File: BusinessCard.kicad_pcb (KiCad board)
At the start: 4 copper layers, 88.9 x 50.8 mm, 80 parts, among them J1 USB_OTG, Q1 2N3904, Q2 2N3904, U1 TLE2426, U10 74HC74, U11 74HC74, U12 74HC74, U13 74HC74, U2 TLV271, U3 LM311, U4 74HC74, U5 INA826, U6 TLV272, U7 4066, U8 TLV272, U9 74HC14

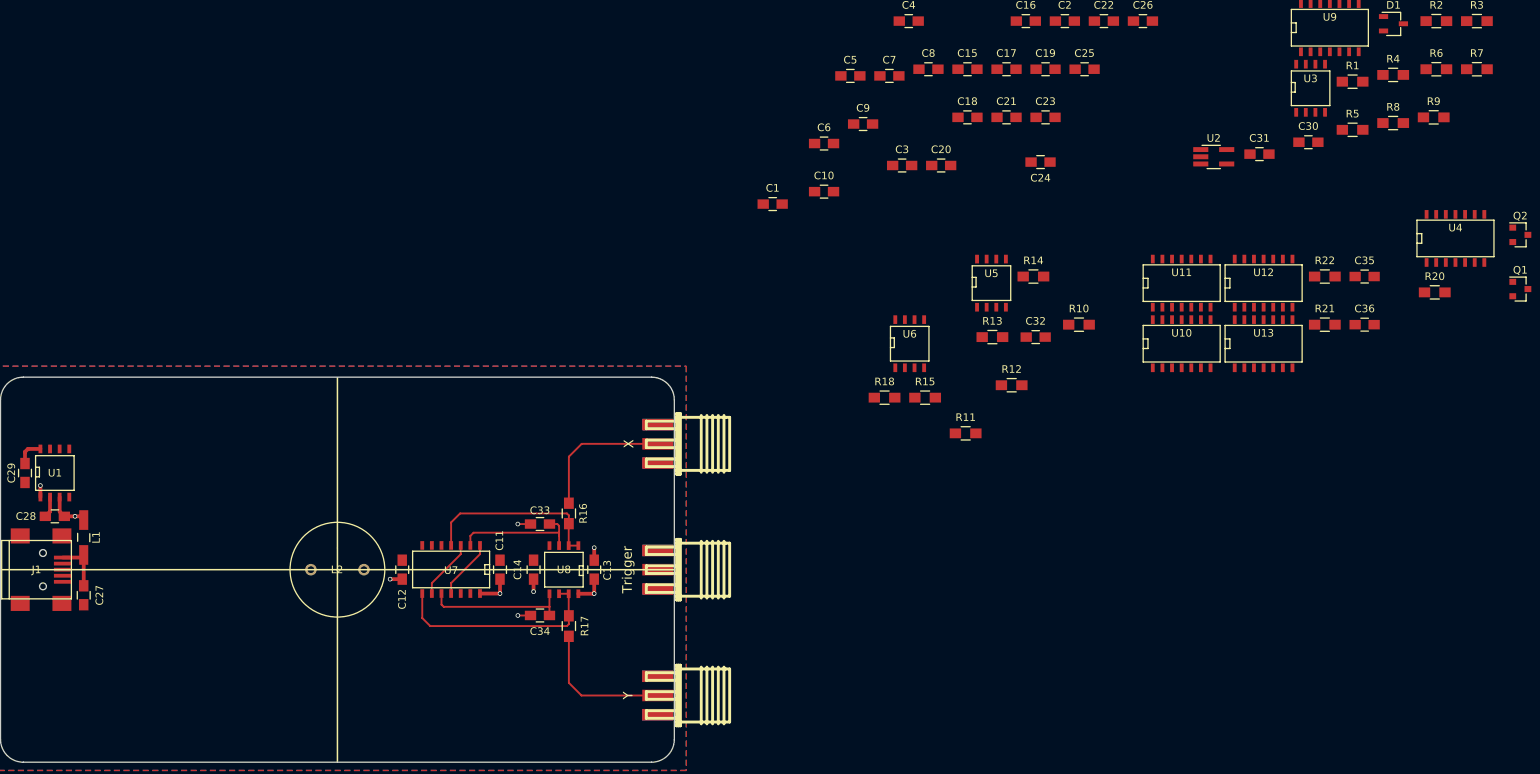
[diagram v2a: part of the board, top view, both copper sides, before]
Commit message: Fractal calculator placed.
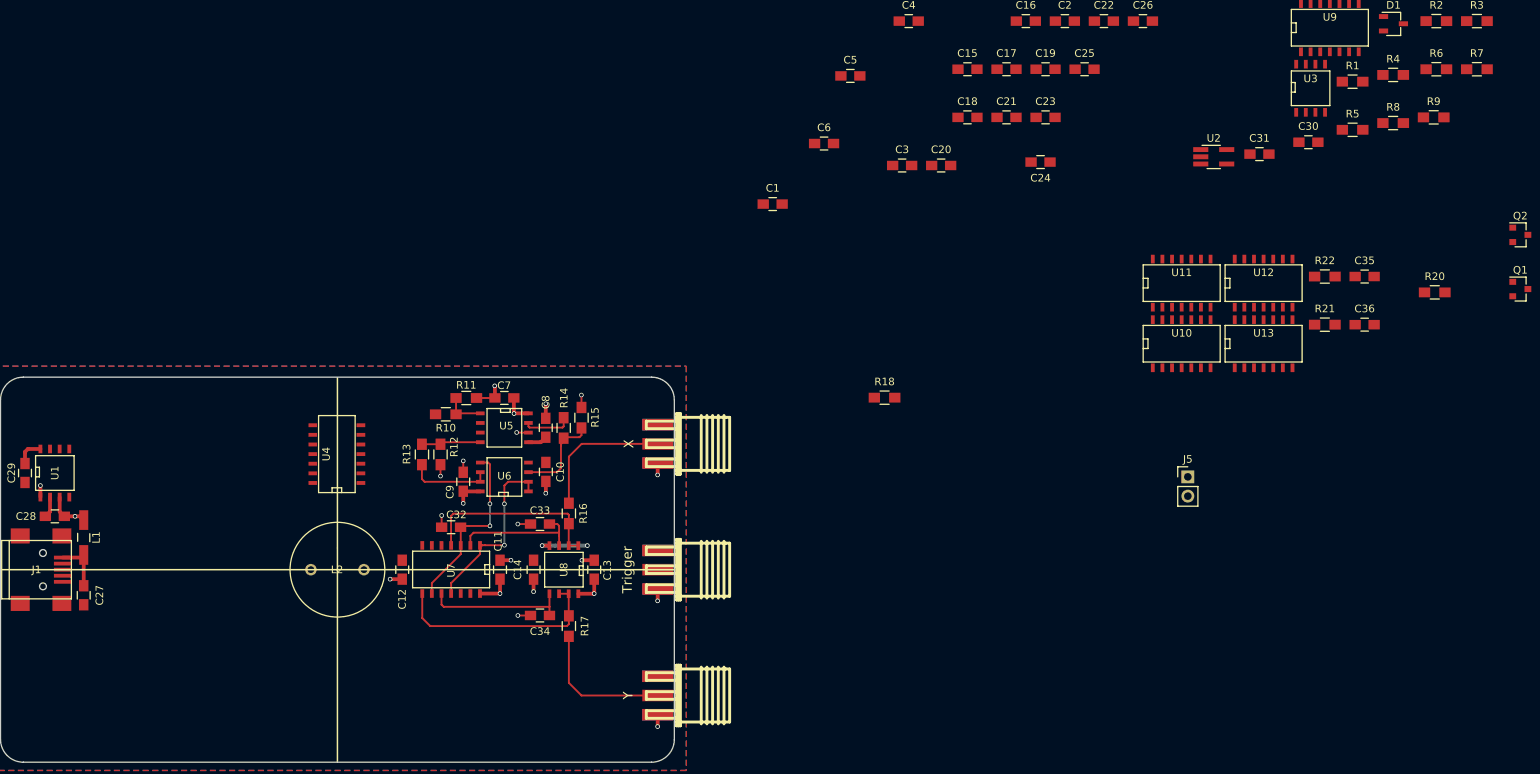
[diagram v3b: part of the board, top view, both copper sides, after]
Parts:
- added J5: RNG, Pin_Headers:Pin_Header_Straight_1x02_Pitch2.54mm, F.Cu at (261.7, 84.5)
- moved U4 150.4 mm to (149.3, 81.5), turned to 90 degrees
- moved R10 84.4 mm to (163.8, 76.2)
- moved C32 81.1 mm to (164.6, 91.1), turned to 180 degrees
- moved R13 76.8 mm to (160.7, 81.5), turned to 270 degrees
- moved R12 75.9 mm to (163.2, 81.5), turned to 270 degrees
- moved C9 70.8 mm to (166.2, 85.1), turned to 90 degrees
- moved C8 69.2 mm to (177.0, 78.0), turned to 270 degrees
- moved U5 67.0 mm to (171.6, 78.0), turned to 270 degrees
- moved C7 66.2 mm to (171.6, 74.0), turned to 180 degrees
- moved R11 66.0 mm to (166.6, 74.0)
- moved R14 65.1 mm to (179.4, 78.0), turned to 270 degrees
- moved U6 56.3 mm to (171.6, 84.5), turned to 90 degrees
- moved C10 52.1 mm to (177.1, 83.8), turned to 90 degrees
- moved R15 45.4 mm to (181.8, 76.7), turned to 90 degrees
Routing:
- net GNDREF: track 9.77 -> 31.6 mm, vias 6 -> 18
- net Net-(C32-Pad1): track 7.93 -> 23.8 mm, vias 0 -> 2
- net Net-(U6-Pad1): track 7.93 -> 23.7 mm, vias 0 -> 2
- net Net-(R14-Pad2): track 0.00 -> 12.1 mm
- net Net-(R13-Pad2): track 0.00 -> 11.1 mm
- net -VDC: track 2.79 -> 12.3 mm, vias 0 -> 2
- net +VDC: track 14.1 -> 22.2 mm, vias 3 -> 5
- net Net-(R12-Pad1): track 0.00 -> 7.81 mm
- net Net-(R14-Pad1): track 0.00 -> 6.38 mm
- net Net-(R10-Pad2): track 0.00 -> 5.40 mm
- net FRACTAL_X: track 24.4 -> 25.0 mm

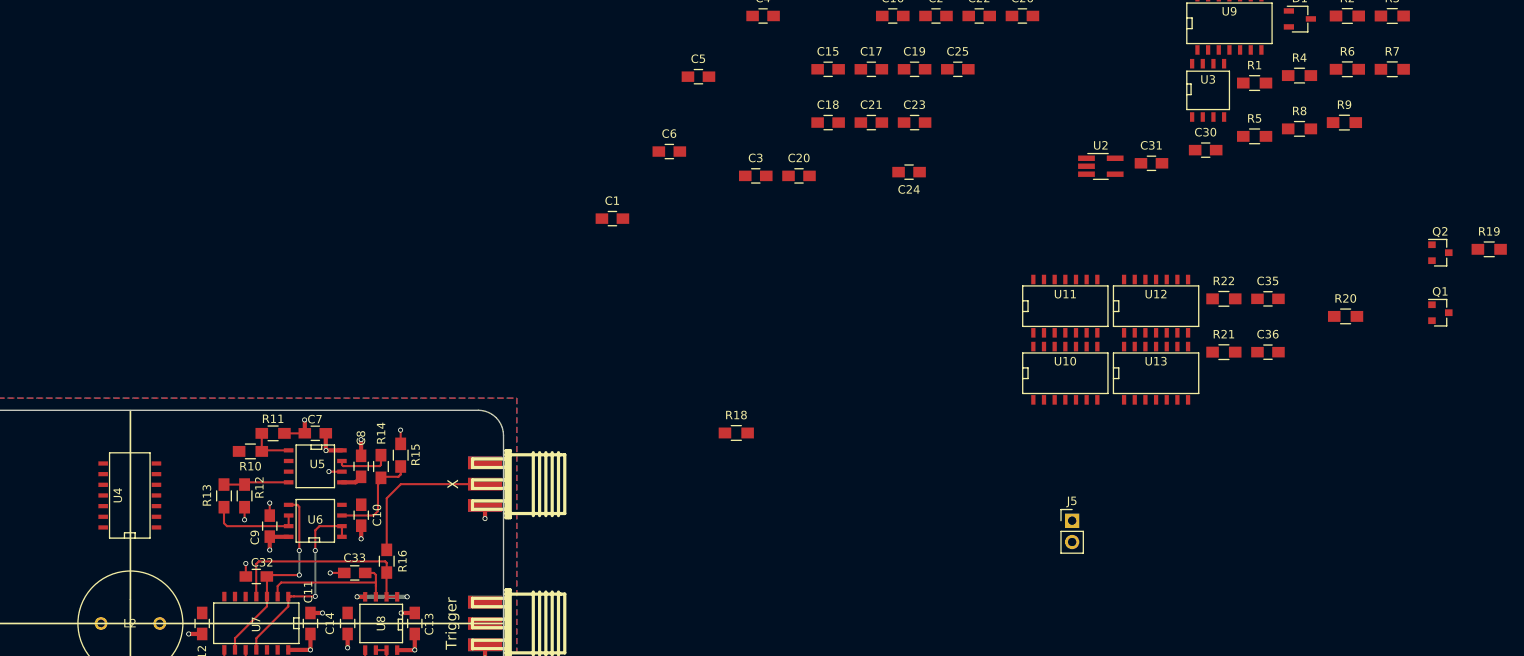
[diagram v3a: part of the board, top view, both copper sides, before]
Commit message: fractal coordinate selector placed.
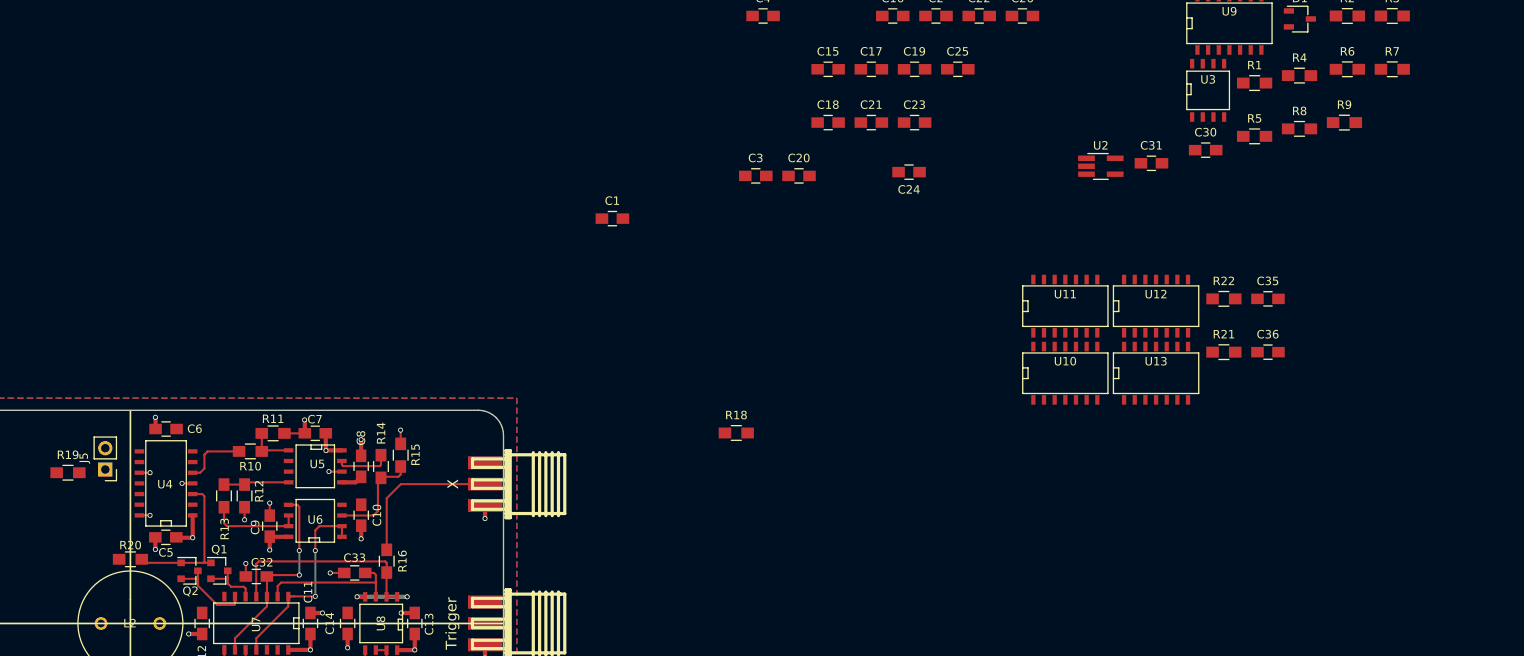
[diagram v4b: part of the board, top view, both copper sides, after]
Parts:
- moved R19 171.4 mm to (142.1, 78.7)
- moved Q2 153.8 mm to (156.6, 90.4)
- moved Q1 148.7 mm to (160.1, 90.4)
- moved R20 147.6 mm to (149.6, 89.1), turned to 180 degrees
- moved J5 115.4 mm to (146.6, 78.4), turned to 180 degrees
- moved C5 83.9 mm to (153.8, 86.4), turned to 180 degrees
- moved C6 68.5 mm to (153.8, 73.5)
- moved U4 4.55 mm to (153.7, 80.0)
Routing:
- net Net-(Q1-Pad1): track 0.00 -> 18.0 mm
- net CLOCK_CYCLE_2: track 0.00 -> 10.2 mm
- net +VDC: track 22.2 -> 30.6 mm, vias 5 -> 9
- net COORDINATE: track 0.00 -> 7.55 mm
- net CLOCK_CYCLE_0: track 0.00 -> 7.10 mm
- net GNDREF: track 31.6 -> 34.4 mm, vias 18 -> 20

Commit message: Started fractal clock placement
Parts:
- moved R7 188.1 mm to (119.0, 82.2), turned to 90 degrees
- moved C20 178.4 mm to (66.1, 115.8)
- moved C21 178.4 mm to (74.8, 109.4)
- moved C22 178.4 mm to (87.6, 96.7)
- moved C23 178.4 mm to (79.9, 109.4)
- moved C19 178.4 mm to (79.9, 103.1)
- moved C24 178.4 mm to (79.2, 115.3)
- moved R9 178.3 mm to (126.2, 96.8), turned to 90 degrees
- moved R3 173.1 mm to (135.9, 79.8), turned to 270 degrees
- moved C26 173.1 mm to (92.8, 82.5)
- moved R2 170.6 mm to (131.7, 75.1)
- moved U12 170.3 mm to (111.3, 115.8)
- moved C35 168.2 mm to (121.4, 96.8), turned to 90 degrees
- moved R8 167.5 mm to (125.5, 75.0)
- moved D1 166.9 mm to (131.3, 79.8), turned to 270 degrees
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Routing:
- net Net-(C31-Pad1): track 0.00 -> 25.7 mm
- net Net-(J5-Pad1): track 0.00 -> 24.7 mm, vias 0 -> 1
- net Net-(R6-Pad1): track 0.00 -> 21.7 mm
- net Net-(C30-Pad1): track 0.00 -> 20.5 mm, vias 0 -> 1
- net GNDREF: track 34.4 -> 52.7 mm, vias 20 -> 31
- net +VDC: track 30.6 -> 48.8 mm, vias 9 -> 14
- net Net-(C35-Pad1): track 0.00 -> 16.4 mm
- net RESET: track 0.00 -> 15.6 mm, vias 0 -> 2
- net CHUA_ATTRACTOR: track 0.00 -> 13.8 mm
- net CLOCK: track 0.00 -> 13.0 mm
- net Net-(R4-Pad1): track 0.00 -> 12.4 mm
- net Net-(R7-Pad2): track 0.00 -> 10.6 mm
- net FRACTAL_TRIGGER: track 0.00 -> 10.5 mm
- net CLOCK_CYCLE_0: track 7.10 -> 14.5 mm
- net Net-(R5-Pad2): track 0.00 -> 6.12 mm
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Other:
- board text added: "Craig Heffner (443) 896-7331 heffnercj@gmail.com"
- board text added: "code-free"
- board text added: "μC"

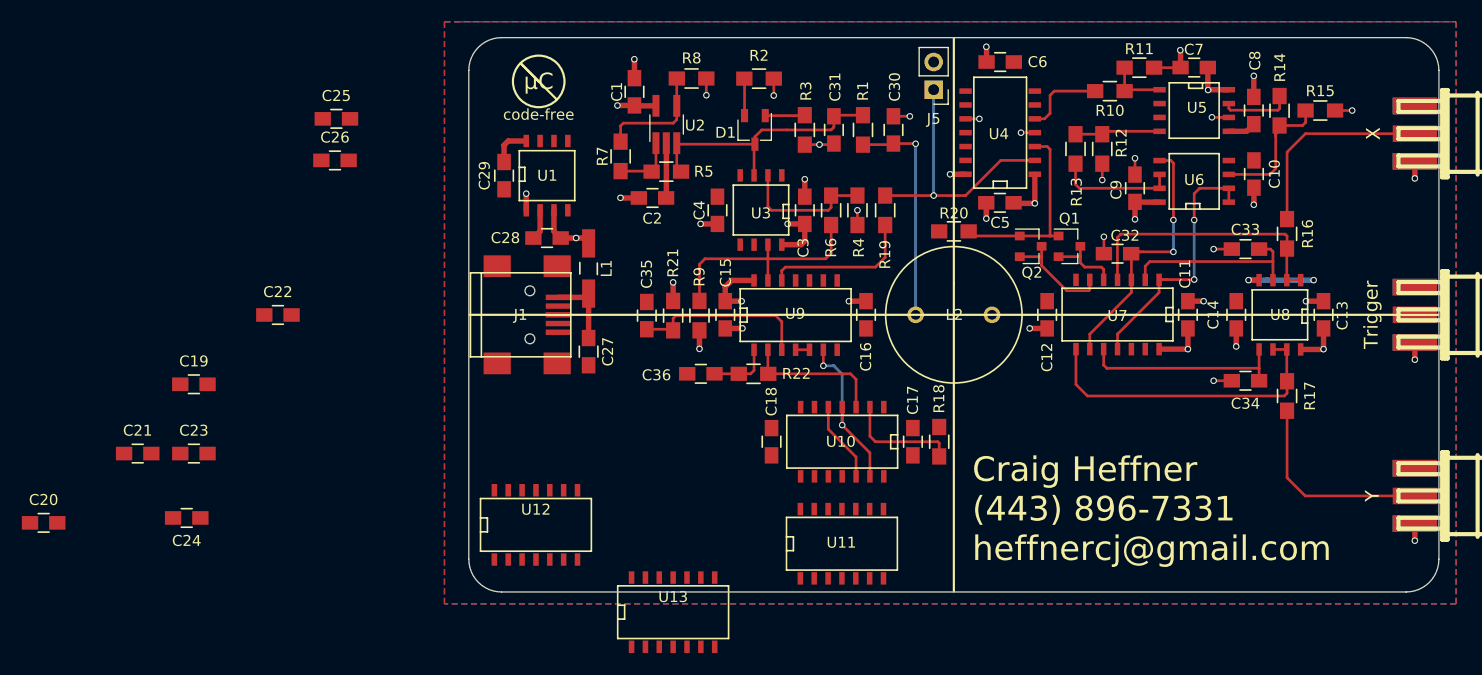
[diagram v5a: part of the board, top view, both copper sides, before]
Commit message: All parts placed, routing incomplete.
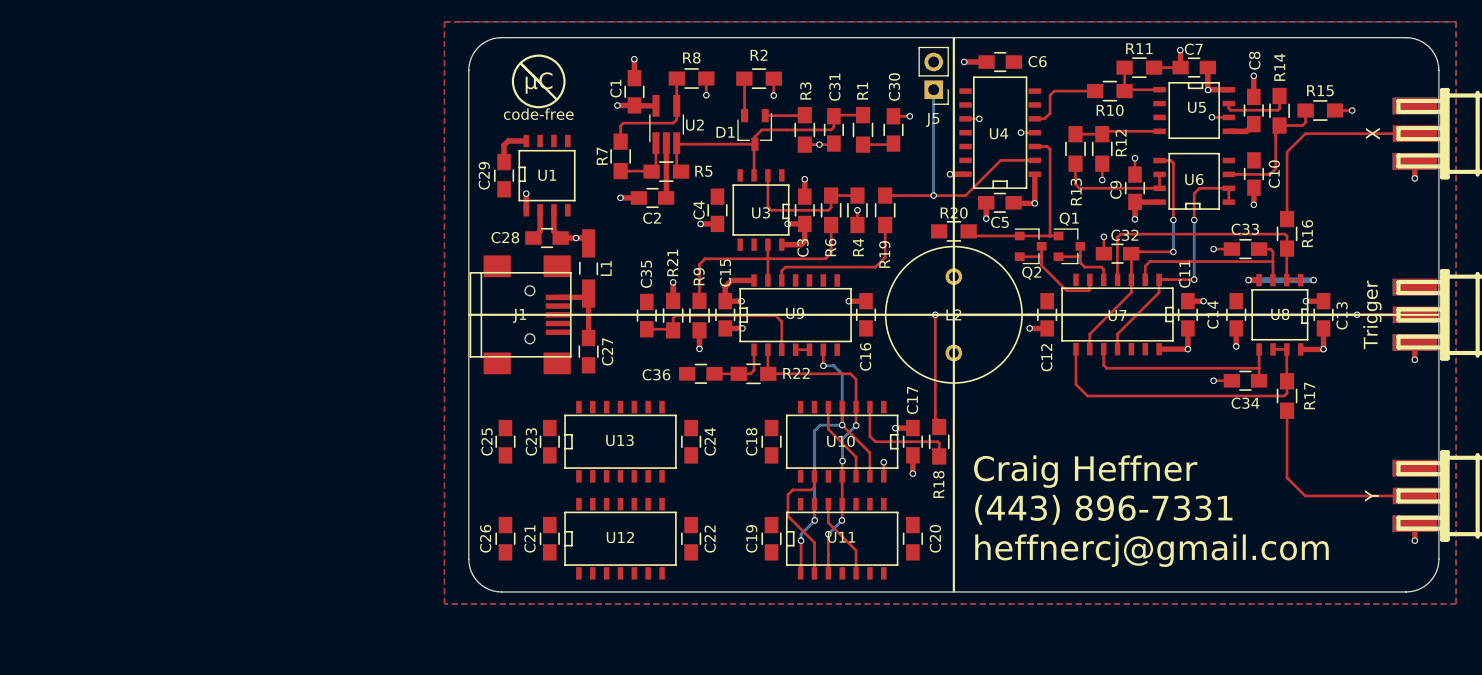
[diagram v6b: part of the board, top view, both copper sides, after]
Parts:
- moved C20 79.7 mm to (145.8, 117.2), turned to 270 degrees
- moved C19 54.8 mm to (132.8, 117.2), turned to 270 degrees
- moved C24 46.8 mm to (125.5, 108.3), turned to 270 degrees
- moved C22 43.1 mm to (125.5, 117.2), turned to 270 degrees
- moved C21 38.6 mm to (112.5, 117.2), turned to 270 degrees
- moved C26 38.0 mm to (108.5, 117.2), turned to 90 degrees
- moved C25 33.4 mm to (108.5, 108.3), turned to 270 degrees
- moved C23 32.6 mm to (112.5, 108.3), turned to 270 degrees
- moved U13 16.3 mm to (119.0, 108.2)
- moved U12 7.85 mm to (119.0, 117.1)
- moved U11 0.46 mm to (139.3, 117.1)
- turned L2 to 270 degrees
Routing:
- net Net-(J4-Pad1): track 0.00 -> 54.4 mm, vias 0 -> 2
- net RESET: track 15.6 -> 33.5 mm, vias 2 -> 4
- net Net-(C30-Pad1): track 20.5 -> 2.84 mm, vias 1 -> 0
- net CLOCK: track 13.0 -> 29.3 mm, vias 0 -> 4
- net Net-(U10-Pad9): track 0.00 -> 11.9 mm
- net CLOCK_CYCLE_1: track 0.00 -> 7.40 mm
- net +VDC: track 48.8 -> 51.7 mm, vias 14 -> 16
- net GNDREF: track 52.7 -> 55.1 mm, vias 31 -> 32
